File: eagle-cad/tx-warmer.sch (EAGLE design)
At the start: 21 parts

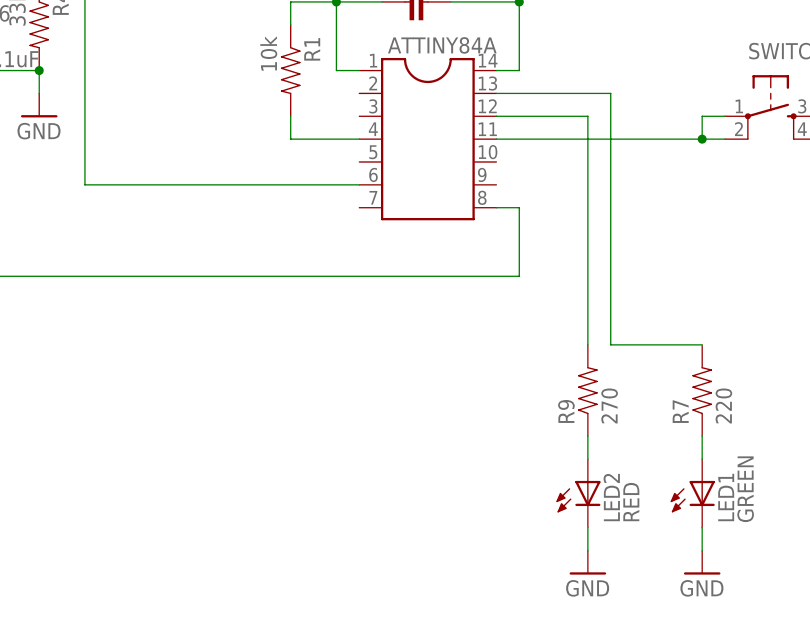
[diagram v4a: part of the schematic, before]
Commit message: Added DIP switches and refactored layout
Switches allow to configure software and reduces firmware variations.
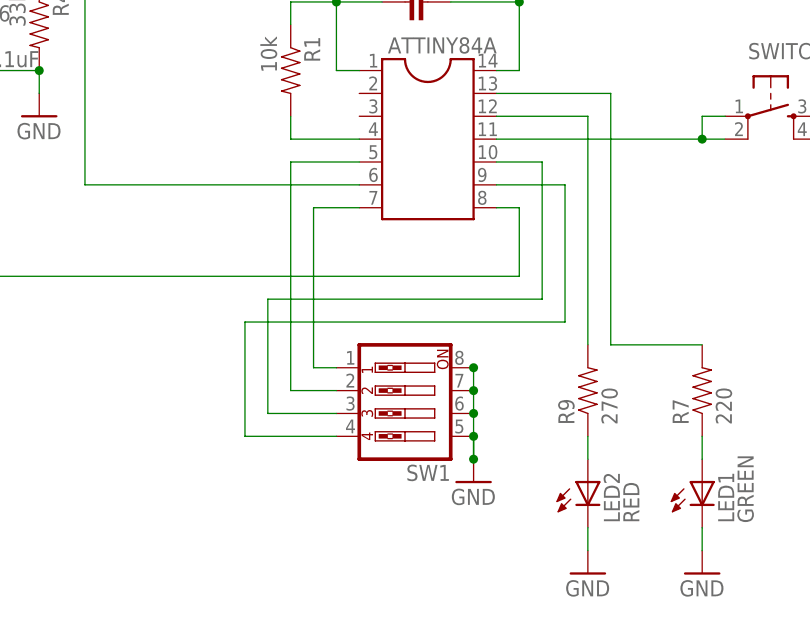
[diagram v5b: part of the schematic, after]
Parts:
- added SW1: (no value), special:SW_DIP-4
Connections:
- new net N$1: ATTINY84A.7, SW1.1
- new net N$2: ATTINY84A.5, SW1.2
- new net N$20: ATTINY84A.9, SW1.4
- new net N$5: ATTINY84A.10, SW1.3
- net GND: now also SW1.5, SW1.6, SW1.7, SW1.8
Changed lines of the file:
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@@
 <part name="H-" library="SparkFun-Connectors" deviceset="M01" device="PTH_2MM"/>
 <part name="LP2950" library="SparkFun-Connectors" deviceset="M03" device="1X03_NO_SILK"/>
+<part name="SW1" library="special" deviceset="SW_DIP-4" device=""/>
+<part name="GND4" library="SparkFun-Aesthetics" deviceset="GND" device=""/>
 </parts>
 <sheets>
@@
 <instance part="H-" gate="G$1" x="-5.08" y="33.02"/>
 <instance part="LP2950" gate="G$1" x="35.56" y="78.74" rot="R270"/>
+<instance part="SW1" gate="A" x="109.22" y="22.86" rot="R180"/>
+<instance part="GND4" gate="1" x="116.84" y="15.24"/>
 </instances>
 <busses>
@@
 <pinref part="GND6" gate="1" pin="GND"/>
 </segment>
+<segment>
+<pinref part="SW1" gate="A" pin="8"/>
+<pinref part="SW1" gate="A" pin="7"/>
+<wire x1="116.84" y1="27.94" x2="116.84" y2="25.4" width="0.1524" layer="91"/>
+<pinref part="SW1" gate="A" pin="6"/>
+<wire x1="116.84" y1="25.4" x2="116.84" y2="22.86" width="0.1524" layer="91"/>
+<pinref part="SW1" gate="A" pin="5"/>
+<wire x1="116.84" y1="22.86" x2="116.84" y2="20.32" width="0.1524" layer="91"/>
+<pinref part="GND4" gate="1" pin="GND"/>
+<wire x1="116.84" y1="20.32" x2="116.84" y2="17.78" width="0.1524" layer="91"/>
+<wire x1="116.84" y1="17.78" x2="116.84" y2="20.32" width="0.1524" layer="91"/>
+<junction x="116.84" y="17.78"/>
+<junction x="116.84" y="27.94"/>
+<junction x="116.84" y="25.4"/>
+<junction x="116.84" y="22.86"/>
+<junction x="116.84" y="20.32"/>
+</segment>
 </net>
 <net name="5V" class="0">
@@
 </segment>
 </net>
+<net name="N$1" class="0">
+<segment>
+<pinref part="SW1" gate="A" pin="1"/>
+<wire x1="101.6" y1="27.94" x2="99.06" y2="27.94" width="0.1524" layer="91"/>
+<wire x1="99.06" y1="27.94" x2="99.06" y2="45.72" width="0.1524" layer="91"/>
+<pinref part="ATTINY84A" gate="G$1" pin="7"/>
+<wire x1="99.06" y1="45.72" x2="104.14" y2="45.72" width="0.1524" layer="91"/>
+</segment>
+</net>
+<net name="N$2" class="0">
+<segment>
+<pinref part="SW1" gate="A" pin="2"/>
+<wire x1="101.6" y1="25.4" x2="96.52" y2="25.4" width="0.1524" layer="91"/>
+<wire x1="96.52" y1="25.4" x2="96.52" y2="50.8" width="0.1524" layer="91"/>
+<pinref part="ATTINY84A" gate="G$1" pin="5"/>
+<wire x1="96.52" y1="50.8" x2="104.14" y2="50.8" width="0.1524" layer="91"/>
+</segment>
+</net>
+<net name="N$5" class="0">
+<segment>
+<wire x1="124.46" y1="50.8" x2="124.46" y2="35.56" width="0.1524" layer="91"/>
+<wire x1="124.46" y1="35.56" x2="93.98" y2="35.56" width="0.1524" layer="91"/>
+<wire x1="93.98" y1="35.56" x2="93.98" y2="22.86" width="0.1524" layer="91"/>
+<pinref part="SW1" gate="A" pin="3"/>
+<wire x1="93.98" y1="22.86" x2="101.6" y2="22.86" width="0.1524" layer="91"/>
+<pinref part="ATTINY84A" gate="G$1" pin="10"/>
+<wire x1="124.46" y1="50.8" x2="119.38" y2="50.8" width="0.1524" layer="91"/>
+</segment>
+</net>
+<net name="N$20" class="0">
+<segment>
+<wire x1="127" y1="33.02" x2="91.44" y2="33.02" width="0.1524" layer="91"/>
+<wire x1="91.44" y1="33.02" x2="91.44" y2="20.32" width="0.1524" layer="91"/>
+<pinref part="SW1" gate="A" pin="4"/>
+<wire x1="91.44" y1="20.32" x2="101.6" y2="20.32" width="0.1524" layer="91"/>
+<wire x1="127" y1="33.02" x2="127" y2="48.26" width="0.1524" layer="91"/>
+<pinref part="ATTINY84A" gate="G$1" pin="9"/>
+<wire x1="127" y1="48.26" x2="119.38" y2="48.26" width="0.1524" layer="91"/>
+</segment>
+</net>

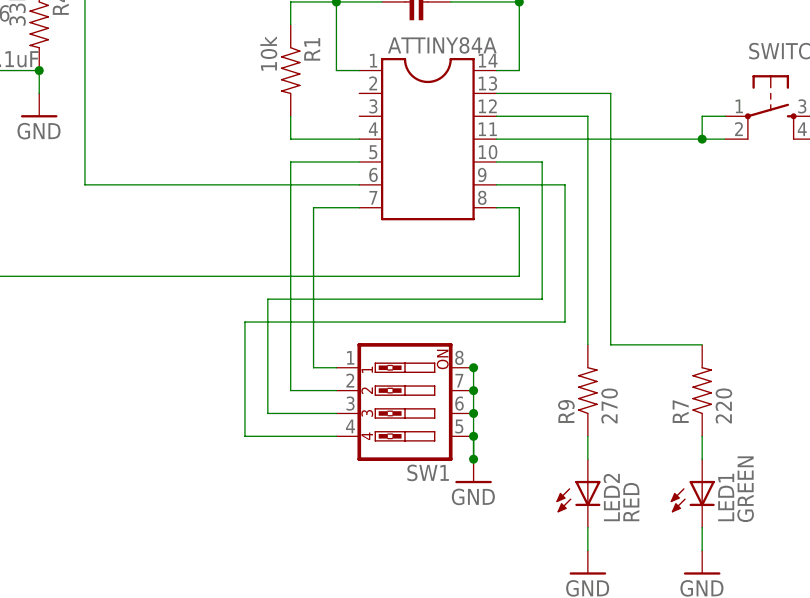
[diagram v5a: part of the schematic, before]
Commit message: Flipped DIP-switches
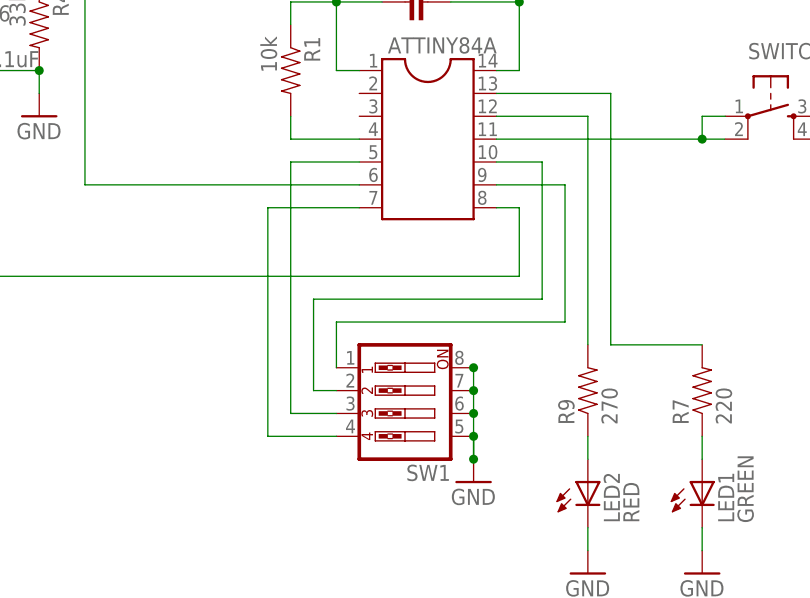
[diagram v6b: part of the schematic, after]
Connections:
- net N$1: now also SW1.4; no longer SW1.1
- net N$2: now also SW1.3; no longer SW1.2
- net N$20: now also SW1.1; no longer SW1.4
- net N$5: now also SW1.2; no longer SW1.3
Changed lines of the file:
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@@
 <net name="N$1" class="0">
 <segment>
-<pinref part="SW1" gate="A" pin="1"/>
-<wire x1="101.6" y1="27.94" x2="99.06" y2="27.94" width="0.1524" layer="91"/>
-<wire x1="99.06" y1="27.94" x2="99.06" y2="45.72" width="0.1524" layer="91"/>
+<wire x1="93.98" y1="20.32" x2="93.98" y2="45.72" width="0.1524" layer="91"/>
 <pinref part="ATTINY84A" gate="G$1" pin="7"/>
-<wire x1="99.06" y1="45.72" x2="104.14" y2="45.72" width="0.1524" layer="91"/>
+<wire x1="93.98" y1="45.72" x2="104.14" y2="45.72" width="0.1524" layer="91"/>
+<pinref part="SW1" gate="A" pin="4"/>
+<wire x1="93.98" y1="20.32" x2="101.6" y2="20.32" width="0.1524" layer="91"/>
 </segment>
 </net>
 <net name="N$2" class="0">
 <segment>
-<pinref part="SW1" gate="A" pin="2"/>
-<wire x1="101.6" y1="25.4" x2="96.52" y2="25.4" width="0.1524" layer="91"/>
-<wire x1="96.52" y1="25.4" x2="96.52" y2="50.8" width="0.1524" layer="91"/>
+<wire x1="96.52" y1="22.86" x2="96.52" y2="50.8" width="0.1524" layer="91"/>
 <pinref part="ATTINY84A" gate="G$1" pin="5"/>
 <wire x1="96.52" y1="50.8" x2="104.14" y2="50.8" width="0.1524" layer="91"/>
+<pinref part="SW1" gate="A" pin="3"/>
+<wire x1="96.52" y1="22.86" x2="101.6" y2="22.86" width="0.1524" layer="91"/>
 </segment>
 </net>
@@
 <segment>
 <wire x1="124.46" y1="50.8" x2="124.46" y2="35.56" width="0.1524" layer="91"/>
-<wire x1="124.46" y1="35.56" x2="93.98" y2="35.56" width="0.1524" layer="91"/>
-<wire x1="93.98" y1="35.56" x2="93.98" y2="22.86" width="0.1524" layer="91"/>
-<pinref part="SW1" gate="A" pin="3"/>
-<wire x1="93.98" y1="22.86" x2="101.6" y2="22.86" width="0.1524" layer="91"/>
+<wire x1="124.46" y1="35.56" x2="99.06" y2="35.56" width="0.1524" layer="91"/>
 <pinref part="ATTINY84A" gate="G$1" pin="10"/>
 <wire x1="124.46" y1="50.8" x2="119.38" y2="50.8" width="0.1524" layer="91"/>
+<wire x1="99.06" y1="35.56" x2="99.06" y2="25.4" width="0.1524" layer="91"/>
+<pinref part="SW1" gate="A" pin="2"/>
+<wire x1="99.06" y1="25.4" x2="101.6" y2="25.4" width="0.1524" layer="91"/>
 </segment>
 </net>
 <net name="N$20" class="0">
 <segment>
-<wire x1="127" y1="33.02" x2="91.44" y2="33.02" width="0.1524" layer="91"/>
-<wire x1="91.44" y1="33.02" x2="91.44" y2="20.32" width="0.1524" layer="91"/>
-<pinref part="SW1" gate="A" pin="4"/>
-<wire x1="91.44" y1="20.32" x2="101.6" y2="20.32" width="0.1524" layer="91"/>
+<wire x1="127" y1="33.02" x2="101.6" y2="33.02" width="0.1524" layer="91"/>
 <wire x1="127" y1="33.02" x2="127" y2="48.26" width="0.1524" layer="91"/>
 <pinref part="ATTINY84A" gate="G$1" pin="9"/>
 <wire x1="127" y1="48.26" x2="119.38" y2="48.26" width="0.1524" layer="91"/>
+<wire x1="101.6" y1="33.02" x2="101.6" y2="27.94" width="0.1524" layer="91"/>
+<pinref part="SW1" gate="A" pin="1"/>
 </segment>
 </net>

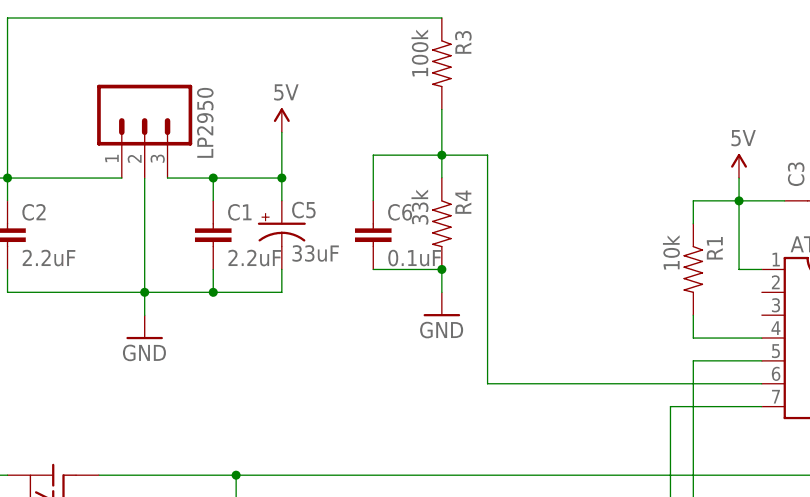
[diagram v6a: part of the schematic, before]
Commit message: Changed capacitors near regulator from 0.1" to 0.2" spacing
To avoid confusion with 0.1uF caps and straight legs sit better at board.
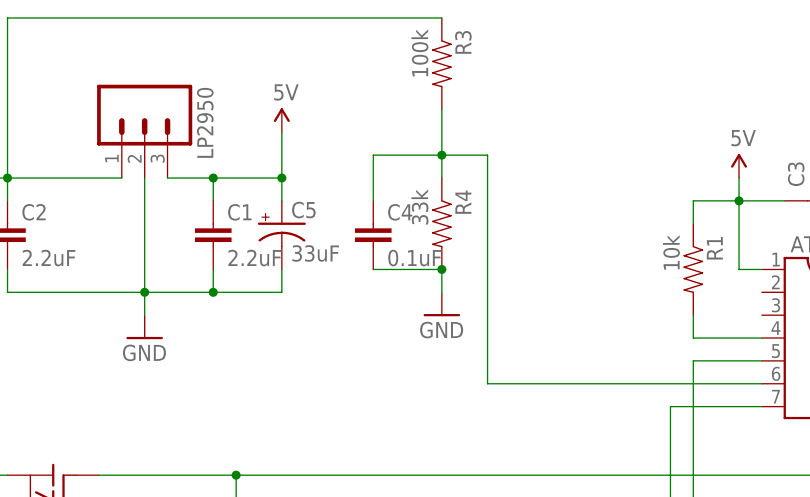
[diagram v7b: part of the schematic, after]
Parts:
- C1, C2: device SparkFun-Passives:CAPEZ -> SparkFun-Passives:CAPPTH1
- renumbered C6 to C4
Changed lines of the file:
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@@
 <part name="LED2" library="SparkFun-LED" deviceset="LED" device="5MM-KIT" value="RED"/>
 <part name="C5" library="SparkFun-Capacitors" deviceset="CAP_POL" device="PTH2" value="33uF"/>
-<part name="C6" library="SparkFun-Passives" deviceset="CAP" device="EZ" value="0.1uF"/>
-<part name="C1" library="SparkFun-Passives" deviceset="CAP" device="EZ" value="2.2uF"/>
-<part name="C2" library="SparkFun-Passives" deviceset="CAP" device="EZ" value="2.2uF"/>
+<part name="C4" library="SparkFun-Passives" deviceset="CAP" device="EZ" value="0.1uF"/>
 <part name="C3" library="SparkFun-Passives" deviceset="CAP" device="EZ" value="0.1uF"/>
 <part name="R1" library="SparkFun-Resistors" deviceset="RESISTOR" device="EZ" value="10k"/>
@@
 <part name="SW1" library="special" deviceset="SW_DIP-4" device=""/>
 <part name="GND4" library="SparkFun-Aesthetics" deviceset="GND" device=""/>
+<part name="C2" library="SparkFun-Passives" deviceset="CAP" device="PTH1" value="2.2uF"/>
+<part name="C1" library="SparkFun-Passives" deviceset="CAP" device="PTH1" value="2.2uF"/>
 </parts>
 <sheets>
@@
 <instance part="LED2" gate="G$1" x="129.54" y="15.24"/>
 <instance part="C5" gate="G$1" x="50.8" y="66.04"/>
-<instance part="C6" gate="G$1" x="60.96" y="63.5"/>
-<instance part="C1" gate="G$1" x="43.18" y="63.5"/>
-<instance part="C2" gate="G$1" x="20.32" y="63.5"/>
+<instance part="C4" gate="G$1" x="60.96" y="63.5"/>
 <instance part="C3" gate="G$1" x="111.76" y="68.58" rot="R90"/>
 <instance part="R1" gate="G$1" x="96.52" y="60.96" rot="R270"/>
@@
 <instance part="SW1" gate="A" x="109.22" y="22.86" rot="R180"/>
 <instance part="GND4" gate="1" x="116.84" y="15.24"/>
+<instance part="C2" gate="G$1" x="20.32" y="63.5"/>
+<instance part="C1" gate="G$1" x="43.18" y="63.5"/>
 </instances>
 <busses>
@@
 <pinref part="R3" gate="G$1" pin="1"/>
 <wire x1="20.32" y1="71.12" x2="33.02" y2="71.12" width="0.1524" layer="91"/>
-<pinref part="C2" gate="G$1" pin="1"/>
 <pinref part="B+" gate="G$1" pin="1"/>
 <pinref part="H+" gate="G$1" pin="1"/>
 <pinref part="LP2950" gate="G$1" pin="1"/>
+<pinref part="C2" gate="G$1" pin="1"/>
 </segment>
 </net>
@@
 <pinref part="C5" gate="G$1" pin="-"/>
 <junction x="43.18" y="58.42"/>
-<pinref part="C1" gate="G$1" pin="2"/>
-<pinref part="C2" gate="G$1" pin="2"/>
 <pinref part="LP2950" gate="G$1" pin="2"/>
 <wire x1="35.56" y1="58.42" x2="35.56" y2="71.12" width="0.1524" layer="91"/>
+<pinref part="C2" gate="G$1" pin="2"/>
+<pinref part="C1" gate="G$1" pin="2"/>
 </segment>
 <segment>
@@
 <wire x1="68.58" y1="60.96" x2="60.96" y2="60.96" width="0.1524" layer="91"/>
 <junction x="68.58" y="60.96"/>
-<pinref part="C6" gate="G$1" pin="2"/>
+<pinref part="C4" gate="G$1" pin="2"/>
 </segment>
 <segment>
@@
 <wire x1="50.8" y1="76.2" x2="50.8" y2="71.12" width="0.1524" layer="91"/>
 <junction x="50.8" y="71.12"/>
-<pinref part="C1" gate="G$1" pin="1"/>
 <pinref part="LP2950" gate="G$1" pin="3"/>
 <wire x1="43.18" y1="71.12" x2="38.1" y2="71.12" width="0.1524" layer="91"/>
 <junction x="43.18" y="71.12"/>
+<pinref part="C1" gate="G$1" pin="1"/>
 </segment>
 </net>
@@
 <wire x1="60.96" y1="68.58" x2="60.96" y2="73.66" width="0.1524" layer="91"/>
 <wire x1="60.96" y1="73.66" x2="68.58" y2="73.66" width="0.1524" layer="91"/>
-<pinref part="C6" gate="G$1" pin="1"/>
-</segment>
-</net>
+<pinref part="C4" gate="G$1" pin="1"/>
+</segment>
+</net>
